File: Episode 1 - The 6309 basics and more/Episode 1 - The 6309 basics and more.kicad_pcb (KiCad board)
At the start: 2 copper layers, 100 x 100 mm, 35 parts, among them J1 100mm_Dev_Board, J2 Barrel_Jack, SW1 Reset, U1 74AHCT541, U2 74AHCT245, U3 HD63C09, U4 74AHCT541, U5 74AHCT541, U6 ATF750C, U7 LMC555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

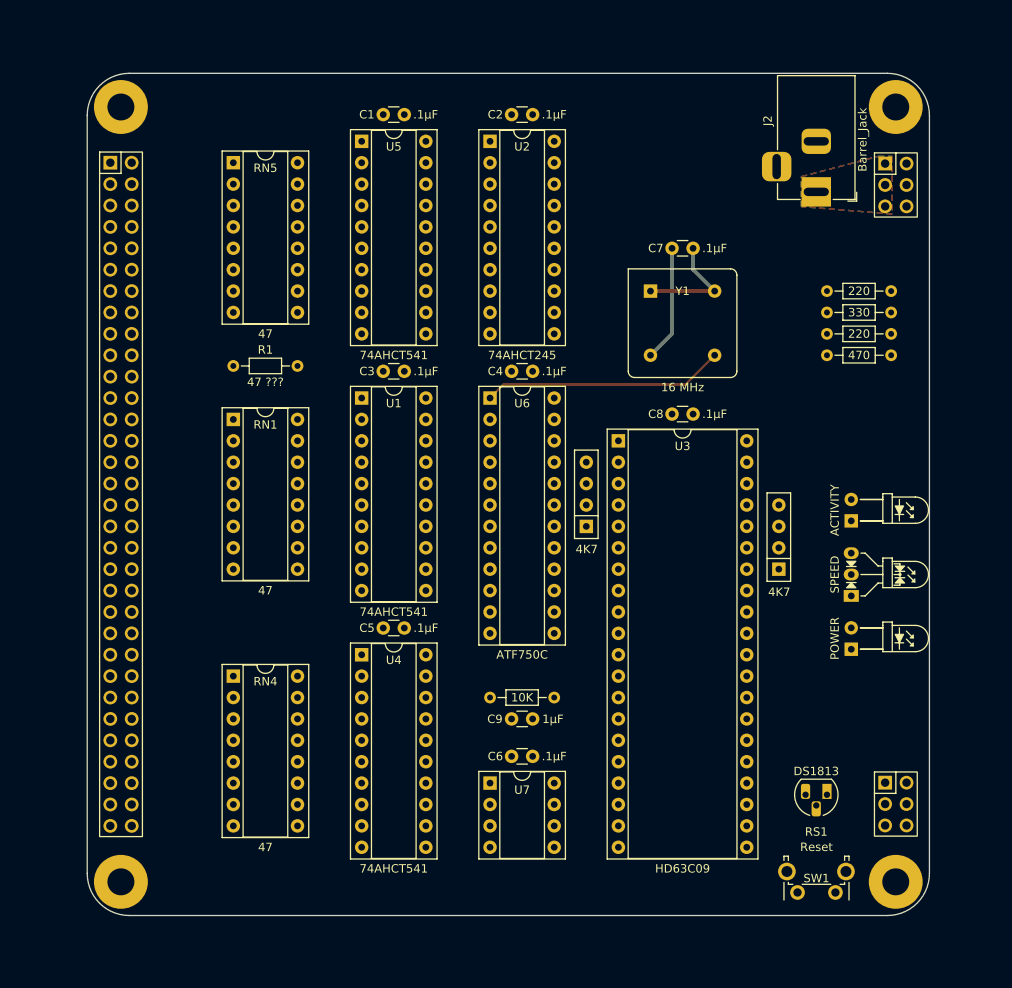
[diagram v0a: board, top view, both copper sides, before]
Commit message: Created the actual PCB
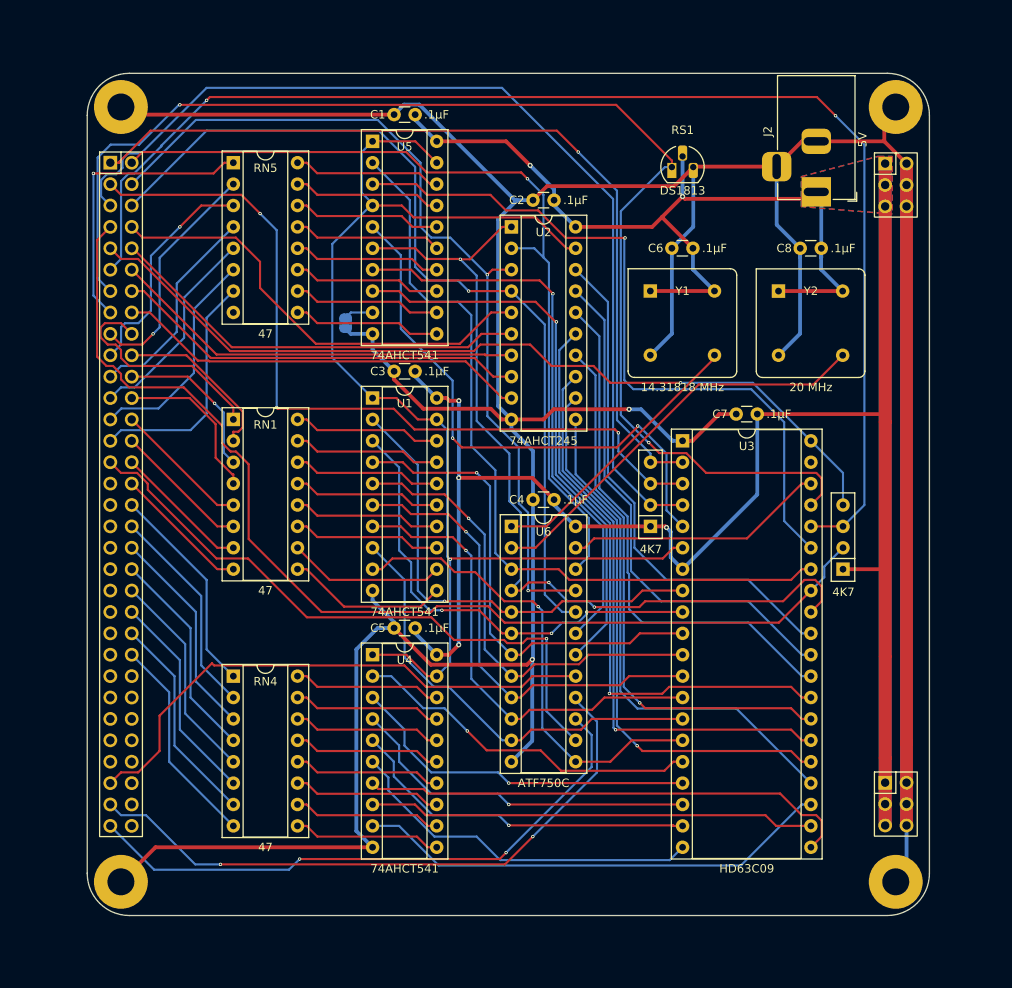
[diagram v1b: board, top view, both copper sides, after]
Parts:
- removed the C6 at (120.0, 125.7)
- removed C9: 1µF, Capacitor_THT:C_Disc_D3.0mm_W1.6mm_P2.50mm
- removed LED1: SPEED, PCM_LED_THT_AKL:LED_D3.0mm_Horizontal_O3.81mm_Z2.0mm_CC
- removed LED2: POWER, PCM_LED_THT_AKL:LED_D3.0mm_Horizontal_O3.81mm_Z10.0mm
- removed LED3: ACTIVITY, PCM_LED_THT_AKL:LED_D3.0mm_Horizontal_O3.81mm_Z10.0mm
- removed R1: 47 ???, Resistor_THT:R_Axial_DIN0204_L3.6mm_D1.6mm_P7.62mm_Horizontal
- removed R2: 330, Resistor_THT:R_Axial_DIN0204_L3.6mm_D1.6mm_P7.62mm_Horizontal
- removed R3, R4: 220, Resistor_THT:R_Axial_DIN0204_L3.6mm_D1.6mm_P7.62mm_Horizontal
- removed R5: 470, Resistor_THT:R_Axial_DIN0204_L3.6mm_D1.6mm_P7.62mm_Horizontal
- removed R6: 10K, Resistor_THT:R_Axial_DIN0204_L3.6mm_D1.6mm_P7.62mm_Horizontal
- removed SW1: Reset, Button_Switch_THT:SW_Tactile_SPST_Angled_PTS645Vx39-2LFS
- removed U7: LMC555, Package_DIP:DIP-8_W7.62mm_Socket
- added C8: .1µF, Capacitor_THT:C_Disc_D3.0mm_W1.6mm_P2.50mm, F.Cu at (154.3, 65.4)
- added NT1: B8, Jumper:SolderJumper-2_P1.3mm_Bridged_RoundedPad1.0x1.5mm, B.Cu at (97.8, 74.3)
- added Y2: 20 MHz, Oscillator:Oscillator_DIP-8, F.Cu at (149.2, 70.5)
- J2: value Barrel_Jack -> 5V
- Y1: value 16 MHz -> 14.31818 MHz
- moved RS1 76.8 mm to (136.5, 55.8), turned to 0 degrees
- moved C4 15.5 mm to (122.5, 95.2)
- moved U6 15.5 mm to (117.5, 98.4)
- moved U2 10.5 mm to (117.5, 62.9)
- moved C2 10.5 mm to (122.5, 59.7)
- moved RN3 7.62 mm to (134.0, 98.4)
- moved C7 7.62 mm to (146.7, 85.1)
- moved RN2 7.62 mm to (156.8, 103.5)
- moved U3 7.62 mm to (137.8, 88.3)
- moved C1 1.29 mm to (106.0, 49.5)
- moved C3 1.29 mm to (106.0, 80.0)
- moved C5 1.29 mm to (106.0, 110.5)
- moved U1 1.29 mm to (101.0, 83.2)
- moved U4 1.29 mm to (101.0, 113.7)
- moved U5 1.29 mm to (101.0, 52.7)
- renumbered C7 to C6, C8 to C7
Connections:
- net /CPU section/16M_{clk} renamed /CPU section/14M_{clk}
- J1 pad 31: ~{MREQ} -> unconnected-(J1-Pin_31-Pad31)
- J1 pad 47: ~{SPD_{reg}} -> unconnected-(J1-Pin_47-Pad47)
- J1 pad 59: unconnected-(J1-Pin_59-Pad59) -> SPD_{LED}^{R}
- J1 pad 61: unconnected-(J1-Pin_61-Pad61) -> SPD_{LED}^{G}
- J1 pad 63: unconnected-(J1-Pin_63-Pad63) -> SPD_{LED}^{B}
- RN5 pad 8: ~{IORQ} -> unconnected-(RN5-R8.1-Pad8)
- U5 pad 9: /CPU section/~{BIORQ} -> Net-(U5-A7)
- U6 pad 10: /CPU section/BA13 -> /CPU section/BA5
- U6 pad 11: /CPU section/BA14 -> /CPU section/BA6
- U6 pad 13: /CPU section/BA15 -> /CPU section/BA7
- U6 pad 14: ~{SPD_{reg}} -> ~{IORQ}
- U6 pad 15: SPD_{LED}^{G} -> SPD_{LED}^{B}
- U6 pad 16: SPD_{LED}^{R} -> SPD_{LED}^{G}
- U6 pad 17: /CPU section/~{UMREQ} -> SPD_{LED}^{R}
- U6 pad 18: /CPU section/~{BIORQ} -> /CPU section/~{BWR}
- U6 pad 19: /CPU section/~{BWR} -> /CPU section/~{BRD}
- U6 pad 2: /CPU section/BE -> /CPU section/20M_{clk}
- U6 pad 20: /CPU section/~{BRD} -> D2
- U6 pad 3: /CPU section/BQ -> /CPU section/BE
- U6 pad 5: /CPU section/BA8 -> /CPU section/BA0
- U6 pad 6: /CPU section/BA9 -> /CPU section/BA1
- U6 pad 7: /CPU section/BA10 -> /CPU section/BA2
- U6 pad 8: /CPU section/BA11 -> /CPU section/BA3
- U6 pad 9: /CPU section/BA12 -> /CPU section/BA4
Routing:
- net GND: track 13.8 -> 583.1 mm, vias 0 -> 2
- net +5V: track 13.8 -> 383.6 mm, vias 0 -> 6
- net ~{MRDY}: track 0.00 -> 156.0 mm, vias 0 -> 2
- net ~{RESET}: track 0.00 -> 153.9 mm, vias 0 -> 2
- net /CPU section/BBA: track 0.00 -> 147.9 mm, vias 0 -> 1
- net ~{BUSRQ}: track 0.00 -> 129.5 mm
- net ~{FIRQ}: track 0.00 -> 116.9 mm
- net D2: track 0.00 -> 105.8 mm, vias 0 -> 1
- net D1: track 0.00 -> 105.7 mm, vias 0 -> 2
- net /CPU section/BR/~{W}: track 0.00 -> 105.1 mm, vias 0 -> 3
- net D0: track 0.00 -> 103.1 mm, vias 0 -> 1
- net ~{HALT}: track 0.00 -> 102.5 mm, vias 0 -> 1
- net ~{NMI}: track 0.00 -> 102.5 mm, vias 0 -> 1
- net ~{IRQ}: track 0.00 -> 96.3 mm, vias 0 -> 3
- net /CPU section/BE: track 0.00 -> 93.7 mm
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
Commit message: Dropped the curved traces
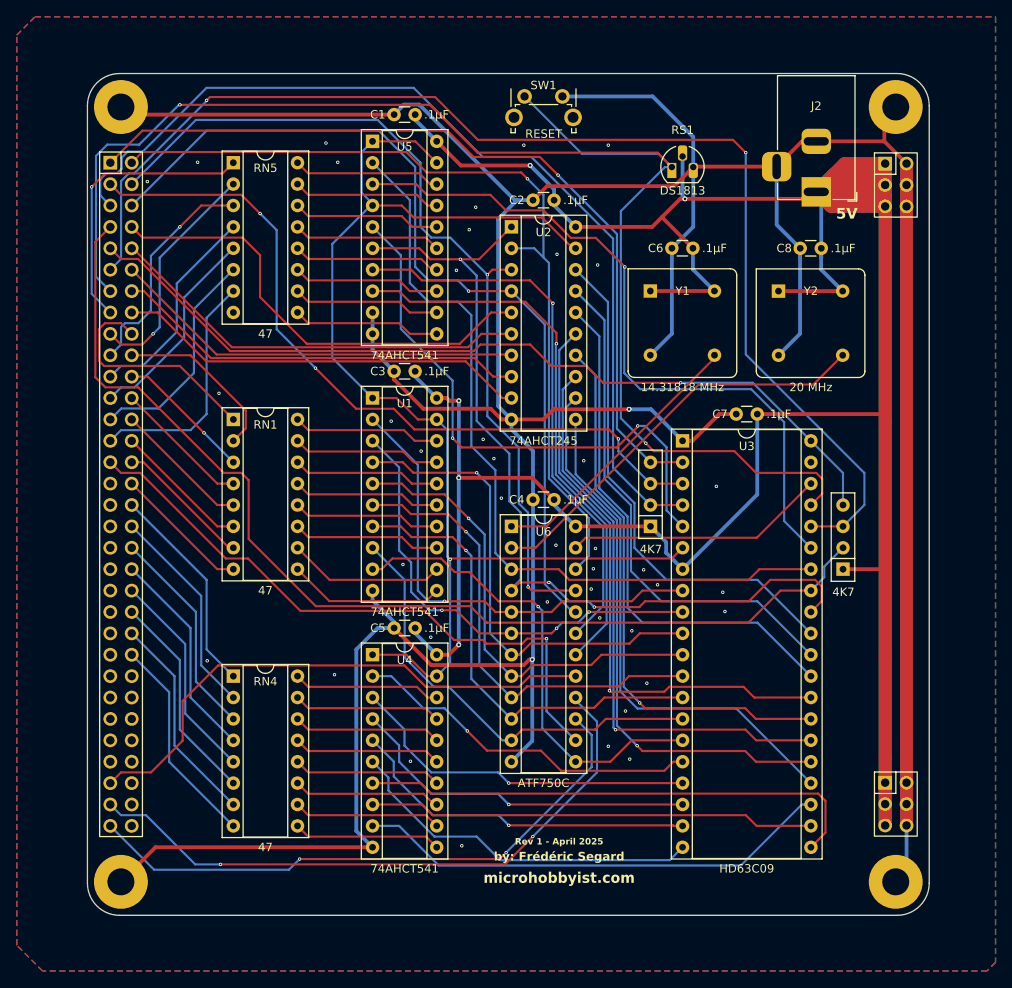
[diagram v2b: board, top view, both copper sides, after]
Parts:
- removed NT1: B8, Jumper:SolderJumper-2_P1.3mm_Bridged_RoundedPad1.0x1.5mm
- added SW1: RESET, Button_Switch_THT:SW_Tactile_SPST_Angled_PTS645Vx39-2LFS, F.Cu at (119.0, 47.4)
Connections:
- U5 pad 9: Net-(U5-A7) -> GND
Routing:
- net +5V: track 383.6 -> 468.5 mm, vias 6 -> 5
- net ~{RESET}: track 153.9 -> 175.1 mm
- net GND: track 583.1 -> 603.3 mm, vias 2 -> 42
- net ~{MRDY}: track 156.0 -> 147.2 mm
- net ~{IRQ}: track 96.3 -> 90.4 mm
- net Net-(U5-A7): track 3.45 -> 0.00 mm
- net ~{NMI}: track 102.5 -> 99.4 mm
- net A3: track 19.2 -> 16.3 mm
- net A2: track 19.1 -> 16.3 mm
- net /CPU section/BQ: track 86.9 -> 84.3 mm
- net ~{FIRQ}: track 116.9 -> 114.4 mm
- net /CPU section/BA13: track 58.9 -> 60.9 mm
- net ~{BUSRQ}: track 129.5 -> 128.0 mm
- net D3: track 54.2 -> 55.3 mm
- net /CPU section/~{BWR}: track 66.9 -> 66.2 mm
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- added copper zone on B.Cu, net GND
- added copper zone on F.Cu, net GND
- removed copper zone on B.Cu, net +5V
- removed copper zone on F.Cu, net +5V
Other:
- board size 100 x 100 mm -> 99.9 x 99.9 mm
- board text added: "Rev 1 - April 2025"
- board text added: "by: Frédéric Segard"
- board text added: "microhobbyist.com"
